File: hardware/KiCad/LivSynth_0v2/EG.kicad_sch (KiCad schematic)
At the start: 29 parts, among them J7 Jumper, Q11 2N3906, Q2 2N3904, Q7 2N3904, Q8 2N3906, SW2 SW_SPST, U6 TL074

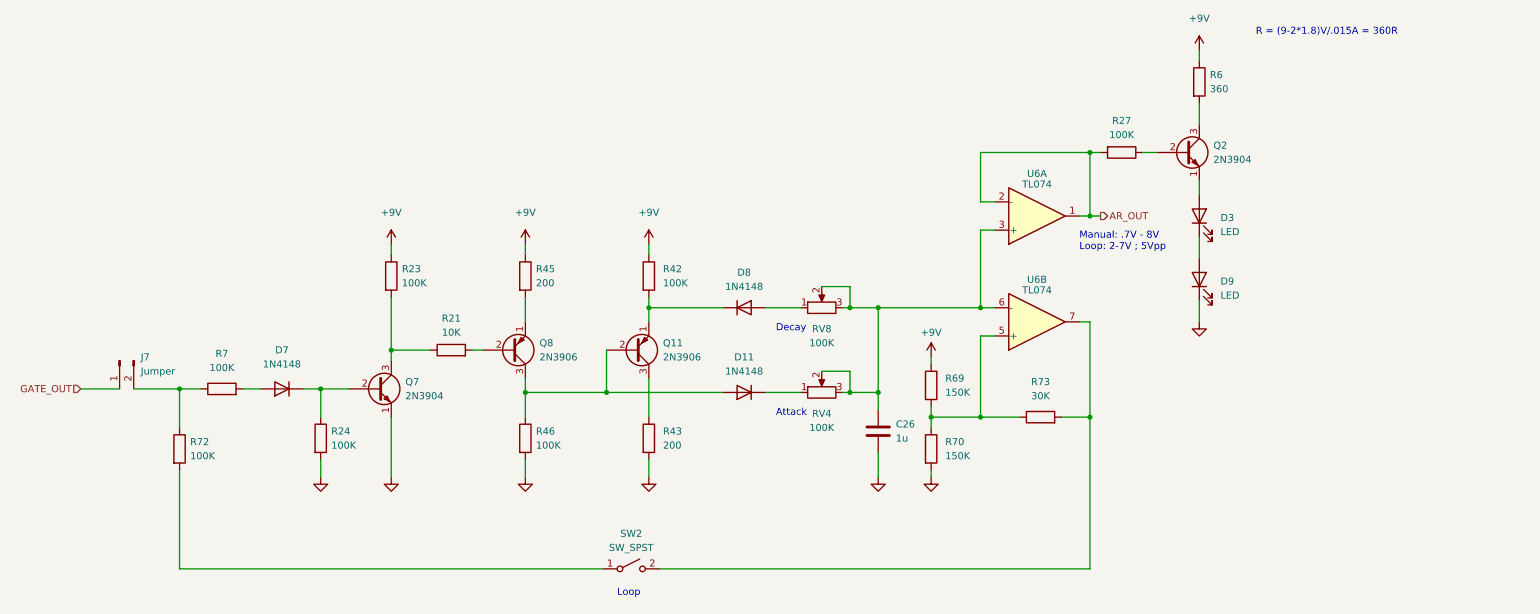
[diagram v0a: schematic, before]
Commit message: Analog redesign:  - Power: Add voltage and current test points  - MCU: use PA11/PA12 for USB DFU interface  - MCU: add NRST reset switch  - Slew: increase portamento cap  - VCO: invert trim pots  - VCF: let resonance kick in earlier  - VCF: invert pots  - VCA: invert trim pot  - EG: full redesign, properly referencing VGND now  - LFO: R61 = 51K  - ModMatrix: add EG attenuverters  - IO: invert pots  - IO: limit output gain for 1W speaker  - IO: connect BTN_SHIFT in gap free order to SR
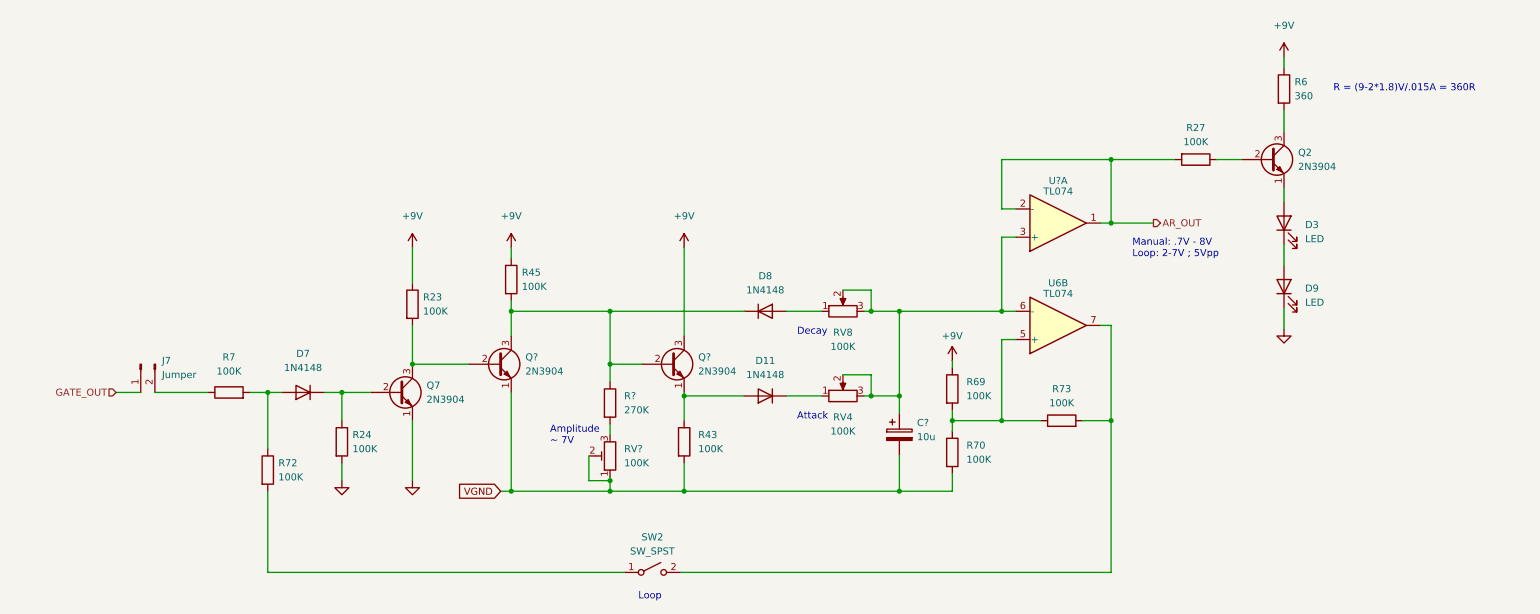
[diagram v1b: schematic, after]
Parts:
- removed C26: 1u, Capacitor_THT:C_Rect_L7.2mm_W2.5mm_P5.00mm_FKS2_FKP2_MKS2_MKP2, symbol Device:C
- removed Q11, Q8: 2N3906, Package_TO_SOT_THT:TO-92_Inline, symbol Transistor_BJT:2N3906
- removed R21: 10K, Resistor_THT:R_Axial_DIN0207_L6.3mm_D2.5mm_P7.62mm_Horizontal, symbol Device:R
- removed R42, R46: 100K, Resistor_THT:R_Axial_DIN0207_L6.3mm_D2.5mm_P7.62mm_Horizontal, symbol Device:R
- removed unit 1 of U6
- added C?: 10u, Capacitor_THT:CP_Radial_D8.0mm_P3.50mm, symbol Device:C_Polarized
- added Q? (x2): 2N3904, Package_TO_SOT_THT:TO-92_Inline, symbol Transistor_BJT:2N3904
- added R?: 270K, Resistor_THT:R_Axial_DIN0207_L6.3mm_D2.5mm_P7.62mm_Horizontal, symbol Device:R
- added RV?: 100K, symbol Device:R_Potentiometer_Trim
- added U?: TL074, Package_SO:SOIC-14_3.9x8.7mm_P1.27mm, symbol Amplifier_Operational:TL074
- R43, R45: value 200 -> 100K
- R69, R70: value 150K -> 100K
- R73: value 30K -> 100K
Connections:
- net +9V: now also Q?.3 (C)
- net AR_OUT: now also U?.1, U?.2 (-)
- net GND: no longer R43.2, R70.2
- net at D8.1 (K): now also R45.2, Q?.2 (B), Q?.3 (C), R?.1
- net at D11.2 (A): now also R43.1, Q?.1 (E)
- net at RV4.2, RV4.3, RV8.2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: now also C?.1, U?.3 (+)
- net at Q7.3 (C), R23.2: now also Q?.2 (B)
- net at D7.2 (A), R7.2: now also R72.1
- net at J7.2 (Pin_2), R7.1: no longer R72.1
- new net: R?.2, RV?.3
- new net VGND: C?.2, Q?.1 (E), R43.2, R70.2, RV?.1, RV?.2
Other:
- note added: "Amplitude ~ 7V"
- moved on the sheet: D11, D3, D7, D8, D9, J7, Q2, Q7, R23, R24, R27, R43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

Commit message: Analog Redesign:  - Power: Build ververse polarity protection using P-Mosfet and Zener Diode      - (https://www.youtube.com/watch?v=Ltx4vovY5Z4 - 1:28)  - Power: Build adjustable buck regulator for 8-9V stable voltage source  - PCB: Add location for order number ("JLCJLCJLCJLC")  - General: Add Tooling Holes for PCB assembly  - PCB: check frontend component layout for symmetry  - VCF: fix sound issues  - PCB: Add SloBlo icon  - PCB: Add switch labels to front side  - EG: test new design  - MCU: Add some debug pins
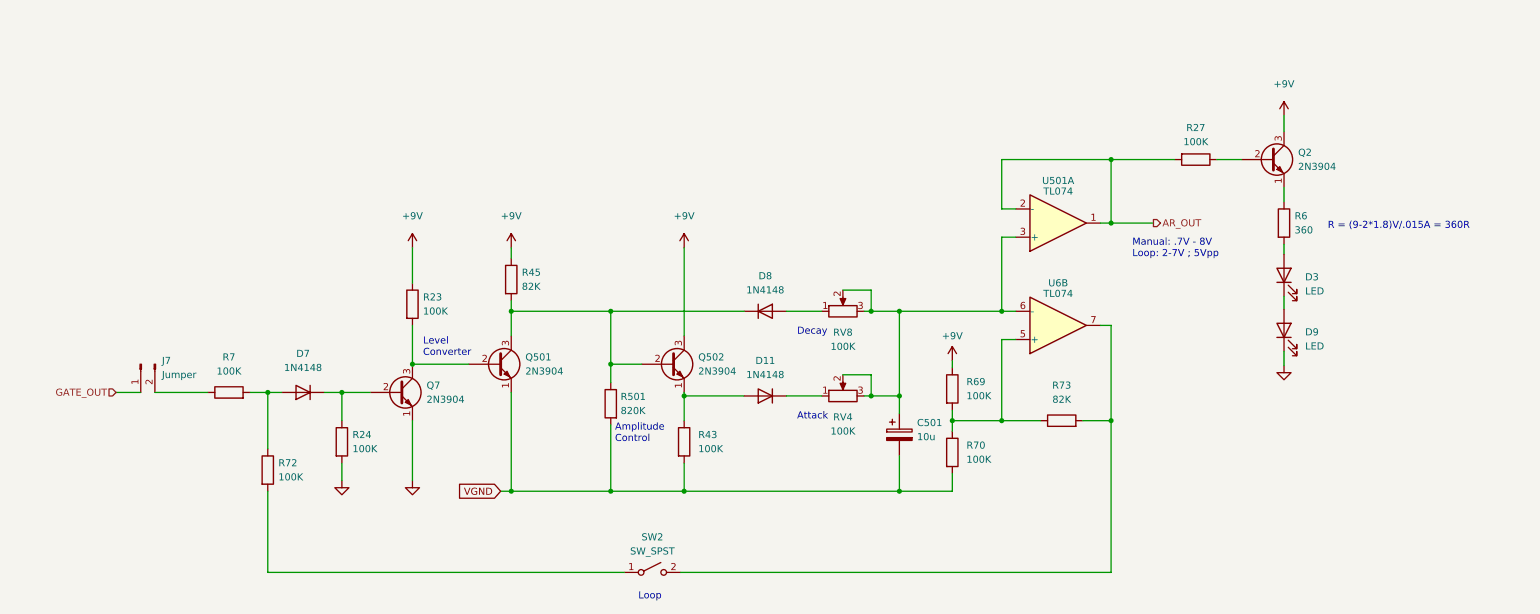
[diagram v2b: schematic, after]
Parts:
- removed RV?: 100K, symbol Device:R_Potentiometer_Trim
- R45, R73: value 100K -> 82K
- R501: renamed from R?; value 270K -> 820K
- U501: renamed from U?; LCSC (none) -> C2057504
- U6: LCSC (none) -> C2057504
- gave numbers to parts that had none: 3
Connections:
- net +9V: now also Q2.3 (C); no longer R6.1
- net VGND: now also R501.2
- net at Q2.1 (E): now also R6.1; no longer D3.2 (A)
- net at R6.2: now also D3.2 (A); no longer Q2.3 (C)
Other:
- note added: "Amplitude Control"
- note added: "Level Converter"
- note removed: "Amplitude ~ 7V"
- moved on the sheet: D3, D9, R6

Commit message: progress 2023-01-21
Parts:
- renumbered U501 to U6
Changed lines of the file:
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@@
   (symbol (lib_id "Amplifier_Operational:TL074") (at 201.93 72.39 0) (mirror x) (unit 1)
     (in_bom yes) (on_board yes)
-    (property "Reference" "U501" (id 0) (at 201.93 64.77 0))
+    (property "Reference" "U6" (id 0) (at 201.93 64.77 0))
     (property "Value" "TL074" (id 1) (at 201.93 66.675 0))
     (property "Footprint" "Package_SO:SOIC-14_3.9x8.7mm_P1.27mm" (id 2) (at 200.66 74.93 0)

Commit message: Geographical reannotate
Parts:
- renumbered C501 to C22, D8 to D11, D3 to D2, D7 to D6, D11 to D7, J7 to J11, Q7 to Q10, Q501 to Q13, Q502 to Q15, R72 to R12, R7 to R13, R45 to R20, R23 to R21, R24 to R32, R27 to R4, R501 to R49, R43 to R51, R73 to R60, R70 to R64, R69 to R66, RV8 to RV10, RV4 to RV6, U6 to U5
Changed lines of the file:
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@@
   (symbol (lib_id "Device:R") (at 121.412 104.902 0) (mirror y) (unit 1)
     (in_bom yes) (on_board yes) (fields_autoplaced)
-    (property "Reference" "R501" (id 0) (at 123.19 103.6319 0)
+    (property "Reference" "R49" (id 0) (at 123.19 103.6319 0)
       (effects (font (size 1.27 1.27)) (justify right))
     )
@@
   (symbol (lib_id "Device:D") (at 149.225 88.265 0) (unit 1)
     (in_bom yes) (on_board yes) (fields_autoplaced)
-    (property "Reference" "D8" (id 0) (at 149.225 81.915 0))
+    (property "Reference" "D11" (id 0) (at 149.225 81.915 0))
     (property "Value" "1N4148" (id 1) (at 149.225 84.455 0))
     (property "Footprint" "Diode_THT:D_DO-35_SOD27_P7.62mm_Horizontal" (id 2) (at 149.225 88.265 0)
@@
   (symbol (lib_id "Transistor_BJT:2N3904") (at 100.965 97.79 0) (unit 1)
     (in_bom yes) (on_board yes) (fields_autoplaced)
-    (property "Reference" "Q501" (id 0) (at 106.045 96.5199 0)
+    (property "Reference" "Q13" (id 0) (at 106.045 96.5199 0)
       (effects (font (size 1.27 1.27)) (justify left))
     )
@@
   (symbol (lib_id "Amplifier_Operational:TL074") (at 201.93 90.805 0) (mirror x) (unit 2)
     (in_bom yes) (on_board yes)
-    (property "Reference" "U6" (id 0) (at 201.93 83.185 0))
+    (property "Reference" "U5" (id 0) (at 201.93 83.185 0))
     (property "Value" "TL074" (id 1) (at 201.93 85.09 0))
     (property "Footprint" "Package_SO:SOIC-14_3.9x8.7mm_P1.27mm" (id 2) (at 200.66 93.345 0)
@@
   (symbol (lib_id "Device:R") (at 85.725 86.995 0) (unit 1)
     (in_bom yes) (on_board yes) (fields_autoplaced)
-    (property "Reference" "R23" (id 0) (at 87.63 85.7249 0)
+    (property "Reference" "R21" (id 0) (at 87.63 85.7249 0)
       (effects (font (size 1.27 1.27)) (justify left))
     )
@@
   (symbol (lib_id "Device:C_Polarized") (at 173.355 110.49 0) (unit 1)
     (in_bom yes) (on_board yes) (fields_autoplaced)
-    (property "Reference" "C501" (id 0) (at 176.53 108.3309 0)
+    (property "Reference" "C22" (id 0) (at 176.53 108.3309 0)
       (effects (font (size 1.27 1.27)) (justify left))
     )
@@
   (symbol (lib_id "Device:D") (at 149.225 103.505 180) (unit 1)
     (in_bom yes) (on_board yes) (fields_autoplaced)
-    (property "Reference" "D11" (id 0) (at 149.225 97.155 0))
+    (property "Reference" "D7" (id 0) (at 149.225 97.155 0))
     (property "Value" "1N4148" (id 1) (at 149.225 99.695 0))
     (property "Footprint" "Diode_THT:D_DO-35_SOD27_P7.62mm_Horizontal" (id 2) (at 149.225 103.505 0)
@@
   (symbol (lib_id "Device:R") (at 103.505 82.55 0) (unit 1)
     (in_bom yes) (on_board yes) (fields_autoplaced)
-    (property "Reference" "R45" (id 0) (at 105.41 81.2799 0)
+    (property "Reference" "R20" (id 0) (at 105.41 81.2799 0)
       (effects (font (size 1.27 1.27)) (justify left))
     )
@@
   (symbol (lib_id "Device:R") (at 226.695 60.96 270) (unit 1)
     (in_bom yes) (on_board yes) (fields_autoplaced)
-    (property "Reference" "R27" (id 0) (at 226.695 55.245 90))
+    (property "Reference" "R4" (id 0) (at 226.695 55.245 90))
     (property "Value" "100K" (id 1) (at 226.695 57.785 90))
     (property "Footprint" "Resistor_THT:R_Axial_DIN0207_L6.3mm_D2.5mm_P7.62mm_Horizontal" (id 2) (at 226.695 59.182 90)
@@
   (symbol (lib_id "Device:R") (at 202.565 107.95 90) (unit 1)
     (in_bom yes) (on_board yes) (fields_autoplaced)
-    (property "Reference" "R73" (id 0) (at 202.565 101.6 90))
+    (property "Reference" "R60" (id 0) (at 202.565 101.6 90))
     (property "Value" "82K" (id 1) (at 202.565 104.14 90))
     (property "Footprint" "Resistor_THT:R_Axial_DIN0207_L6.3mm_D2.5mm_P7.62mm_Horizontal" (id 2) (at 202.565 109.728 90)
@@
   (symbol (lib_id "Transistor_BJT:2N3904") (at 83.185 102.87 0) (unit 1)
     (in_bom yes) (on_board yes) (fields_autoplaced)
-    (property "Reference" "Q7" (id 0) (at 88.265 101.5999 0)
+    (property "Reference" "Q10" (id 0) (at 88.265 101.5999 0)
       (effects (font (size 1.27 1.27)) (justify left))
     )
@@
   (symbol (lib_id "Device:R") (at 73.025 111.76 0) (unit 1)
     (in_bom yes) (on_board yes) (fields_autoplaced)
-    (property "Reference" "R24" (id 0) (at 74.93 110.4899 0)
+    (property "Reference" "R32" (id 0) (at 74.93 110.4899 0)
       (effects (font (size 1.27 1.27)) (justify left))
     )
@@
   (symbol (lib_id "Device:D") (at 66.04 102.87 180) (unit 1)
     (in_bom yes) (on_board yes) (fields_autoplaced)
-    (property "Reference" "D7" (id 0) (at 66.04 95.885 0))
+    (property "Reference" "D6" (id 0) (at 66.04 95.885 0))
     (property "Value" "1N4148" (id 1) (at 66.04 98.425 0))
     (property "Footprint" "Diode_THT:D_DO-35_SOD27_P7.62mm_Horizontal" (id 2) (at 66.04 102.87 0)
@@
   (symbol (lib_id "Device:R_Potentiometer") (at 163.195 88.265 90) (unit 1)
     (in_bom yes) (on_board yes) (fields_autoplaced)
-    (property "Reference" "RV8" (id 0) (at 163.195 92.075 90))
+    (property "Reference" "RV10" (id 0) (at 163.195 92.075 90))
     (property "Value" "100K" (id 1) (at 163.195 94.615 90))
     (property "Footprint" "SloBlo:RV141F-40-20BL" (id 2) (at 163.195 88.265 0)
@@
   (symbol (lib_id "Transistor_BJT:2N3904") (at 132.08 97.79 0) (unit 1)
     (in_bom yes) (on_board yes) (fields_autoplaced)
-    (property "Reference" "Q502" (id 0) (at 137.16 96.5199 0)
+    (property "Reference" "Q15" (id 0) (at 137.16 96.5199 0)
       (effects (font (size 1.27 1.27)) (justify left))
     )
@@
   (symbol (lib_id "Device:R") (at 182.88 102.235 0) (unit 1)
     (in_bom yes) (on_board yes) (fields_autoplaced)
-    (property "Reference" "R69" (id 0) (at 185.42 100.9649 0)
+    (property "Reference" "R66" (id 0) (at 185.42 100.9649 0)
       (effects (font (size 1.27 1.27)) (justify left))
     )
@@
   (symbol (lib_id "Device:LED") (at 242.57 81.788 90) (unit 1)
     (in_bom yes) (on_board yes) (fields_autoplaced)
-    (property "Reference" "D3" (id 0) (at 246.38 82.1054 90)
+    (property "Reference" "D2" (id 0) (at 246.38 82.1054 90)
       (effects (font (size 1.27 1.27)) (justify right))
     )
@@
   (symbol (lib_id "Device:R") (at 59.69 116.84 0) (unit 1)
     (in_bom yes) (on_board yes) (fields_autoplaced)
-    (property "Reference" "R72" (id 0) (at 61.595 115.5699 0)
+    (property "Reference" "R12" (id 0) (at 61.595 115.5699 0)
       (effects (font (size 1.27 1.27)) (justify left))
     )
@@
   (symbol (lib_id "Connector:Conn_01x02_Male") (at 36.83 97.79 90) (mirror x) (unit 1)
     (in_bom yes) (on_board yes) (fields_autoplaced)
-    (property "Reference" "J7" (id 0) (at 40.64 97.1549 90)
+    (property "Reference" "J11" (id 0) (at 40.64 97.1549 90)
       (effects (font (size 1.27 1.27)) (justify right))
     )
@@
   (symbol (lib_id "Device:R") (at 52.705 102.87 90) (unit 1)
     (in_bom yes) (on_board yes) (fields_autoplaced)
-    (property "Reference" "R7" (id 0) (at 52.705 96.52 90))
+    (property "Reference" "R13" (id 0) (at 52.705 96.52 90))
     (property "Value" "100K" (id 1) (at 52.705 99.06 90))
     (property "Footprint" "Resistor_THT:R_Axial_DIN0207_L6.3mm_D2.5mm_P7.62mm_Horizontal" (id 2) (at 52.705 104.648 90)
@@
   (symbol (lib_id "Device:R") (at 182.88 113.665 0) (unit 1)
     (in_bom yes) (on_board yes) (fields_autoplaced)
-    (property "Reference" "R70" (id 0) (at 185.42 112.3949 0)
+    (property "Reference" "R64" (id 0) (at 185.42 112.3949 0)
       (effects (font (size 1.27 1.27)) (justify left))
     )
@@
   (symbol (lib_id "Device:R_Potentiometer") (at 163.195 103.505 90) (unit 1)
     (in_bom yes) (on_board yes) (fields_autoplaced)
-    (property "Reference" "RV4" (id 0) (at 163.195 107.315 90))
+    (property "Reference" "RV6" (id 0) (at 163.195 107.315 90))
     (property "Value" "100K" (id 1) (at 163.195 109.855 90))
     (property "Footprint" "SloBlo:RV141F-40-20BL" (id 2) (at 163.195 103.505 0)
@@
   (symbol (lib_id "Device:R") (at 134.62 111.76 0) (unit 1)
     (in_bom yes) (on_board yes) (fields_autoplaced)
-    (property "Reference" "R43" (id 0) (at 137.16 110.4899 0)
+    (property "Reference" "R51" (id 0) (at 137.16 110.4899 0)
       (effects (font (size 1.27 1.27)) (justify left))
     )
@@
   (symbol (lib_id "Amplifier_Operational:TL074") (at 201.93 72.39 0) (mirror x) (unit 1)
     (in_bom yes) (on_board yes)
-    (property "Reference" "U6" (id 0) (at 201.93 64.77 0))
+    (property "Reference" "U5" (id 0) (at 201.93 64.77 0))
     (property "Value" "TL074" (id 1) (at 201.93 66.675 0))
     (property "Footprint" "Package_SO:SOIC-14_3.9x8.7mm_P1.27mm" (id 2) (at 200.66 74.93 0)

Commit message: Modify toggle switches (footprint and 3D model) Align R value designators Add JLC component placement checkup file
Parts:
- SW2: footprint SloBlo:SW_Toggle_MS500C -> SloBlo:SW_Toggle_MS500
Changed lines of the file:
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@@
     (property "Reference" "SW2" (id 0) (at 128.905 128.905 0))
     (property "Value" "SW_SPST" (id 1) (at 128.905 131.445 0))
-    (property "Footprint" "SloBlo:SW_Toggle_MS500C" (id 2) (at 128.905 135.255 0)
+    (property "Footprint" "SloBlo:SW_Toggle_MS500" (id 2) (at 128.905 135.255 0)
       (effects (font (size 1.27 1.27)) hide)
     )
-    (property "Datasheet" "~" (id 3) (at 128.905 135.255 0)
+    (property "Datasheet" "" (id 3) (at 128.905 135.255 0)
       (effects (font (size 1.27 1.27)) hide)
     )

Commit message: Create new 0v3 folder
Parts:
- SW2: footprint SloBlo:SW_Toggle_MS500 -> SloBlo:SW_Toggle_MS500C
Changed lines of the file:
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@@
     (property "Reference" "SW2" (id 0) (at 128.905 128.905 0))
     (property "Value" "SW_SPST" (id 1) (at 128.905 131.445 0))
-    (property "Footprint" "SloBlo:SW_Toggle_MS500" (id 2) (at 128.905 135.255 0)
+    (property "Footprint" "SloBlo:SW_Toggle_MS500C" (id 2) (at 128.905 135.255 0)
       (effects (font (size 1.27 1.27)) hide)
     )
-    (property "Datasheet" "" (id 3) (at 128.905 135.255 0)
+    (property "Datasheet" "~" (id 3) (at 128.905 135.255 0)
       (effects (font (size 1.27 1.27)) hide)
     )

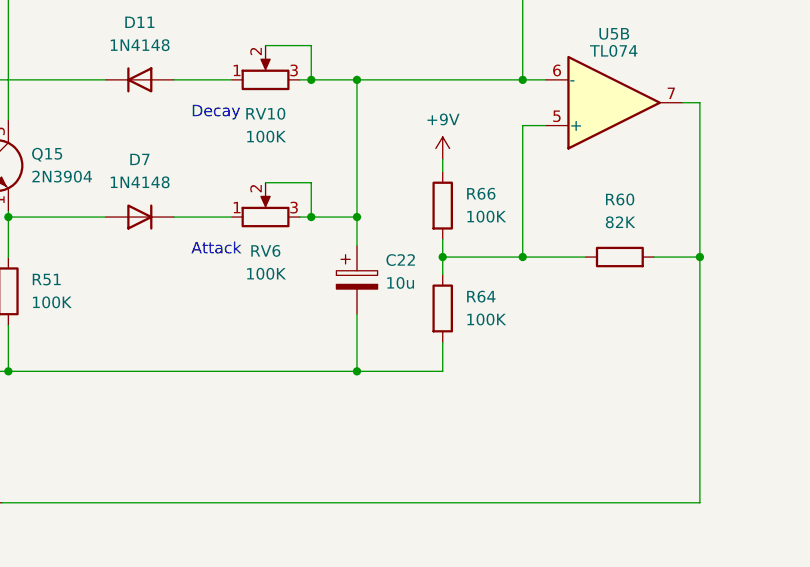
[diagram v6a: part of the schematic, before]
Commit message: Reduce EG cap to 4u7 Reduce LFO cap to 220n VCO R23: 470K, C13: 10n
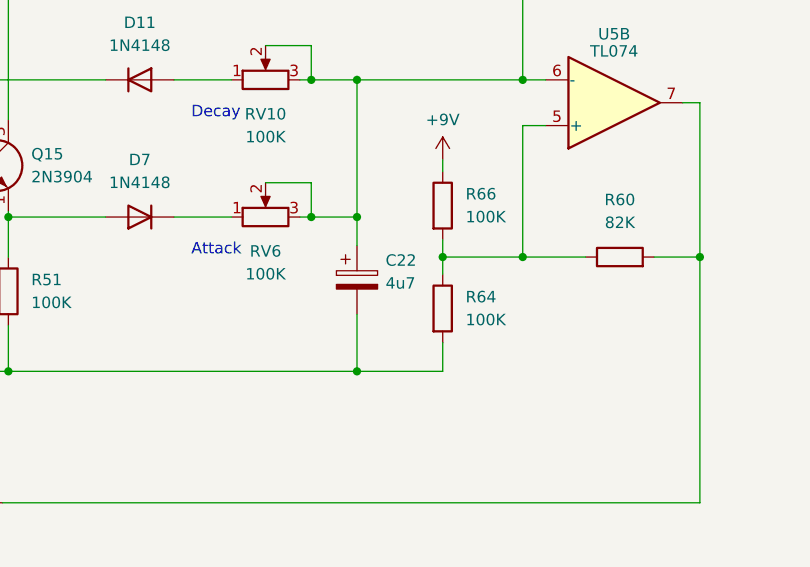
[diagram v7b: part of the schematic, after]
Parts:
- C22: value 10u -> 4u7
- SW2: footprint SloBlo:SW_Toggle_MS500C -> SloBlo:SW_Toggle_MS500
